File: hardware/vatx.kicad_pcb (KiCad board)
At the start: 2 copper layers, 50 x 50.1 mm, 31 parts, among them J1 USB, P1 CONN_10X2, P2 CONN_01X05, P3 CONN_1, P4 CONN_1, P5 CONN_1, P6 CONN_1, P7 CONN_1, P8 CONN_01X03, SW1 SWITCH_INV, U1 LM317T, U2 OPTO-TRANSISTOR4

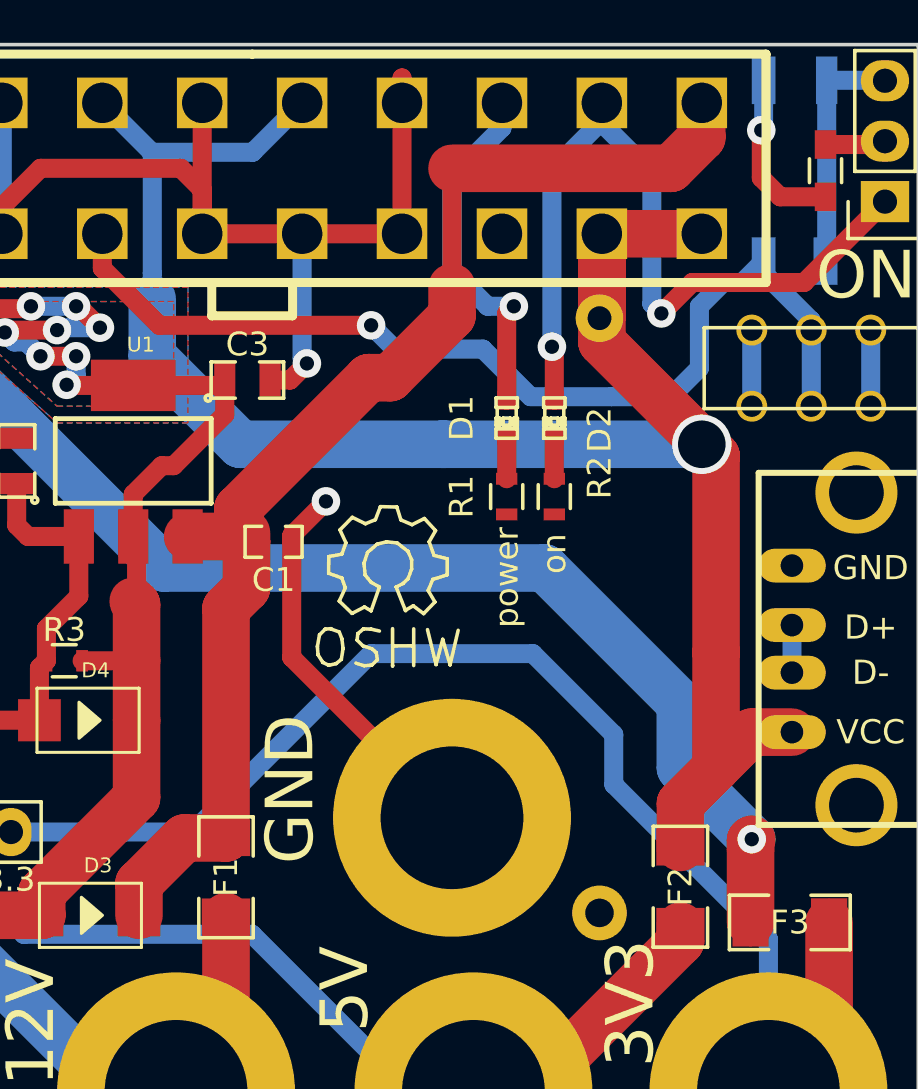
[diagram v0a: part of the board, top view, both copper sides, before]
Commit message: V2.2 bugfix & enhancement * potentiometer connection * power/on silkscreen * more 0.8 traces for power traces (+12V, +5V) * more via for power traces (+5V, +3.3V)
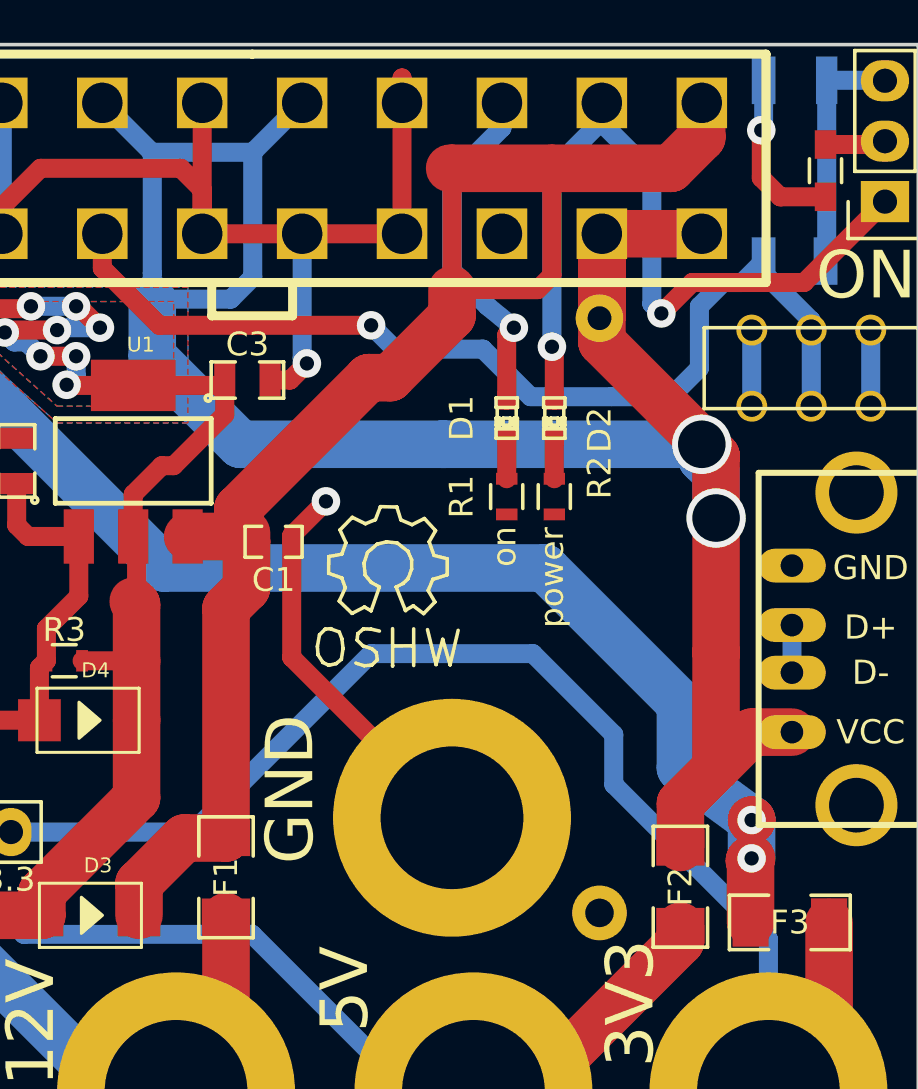
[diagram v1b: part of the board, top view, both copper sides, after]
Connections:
- P1 pad 16: -5V -> (no net)
- P1 pad 4: -12V -> (no net)
- RV1 pad 2: Net-(RV1-Pad2) -> GND
- RV1 pad 3: GND -> (no net)
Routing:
- net +5V: track 84.2 -> 97.5 mm, vias 1 -> 2
- net +12V: track 55.3 -> 64.3 mm
- net POK: track 15.2 -> 14.6 mm
- net +3.3V: track 66.9 -> 67.3 mm, vias 1 -> 2
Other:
- board text added: "vATX v2.3"
- board text removed: "vATX v2.2"
